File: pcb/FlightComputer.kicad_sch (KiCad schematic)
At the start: 80 parts, among them J1 USB4105-GF-A, J2 MOTOR L, J3 MOTOR R, J4 LED L, J7 SERVO R, J8 SERVO R, Q1 DMG3415U, Q2 Si2319CDS, Q3 Si2319CDS, Q4 MMBT3904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

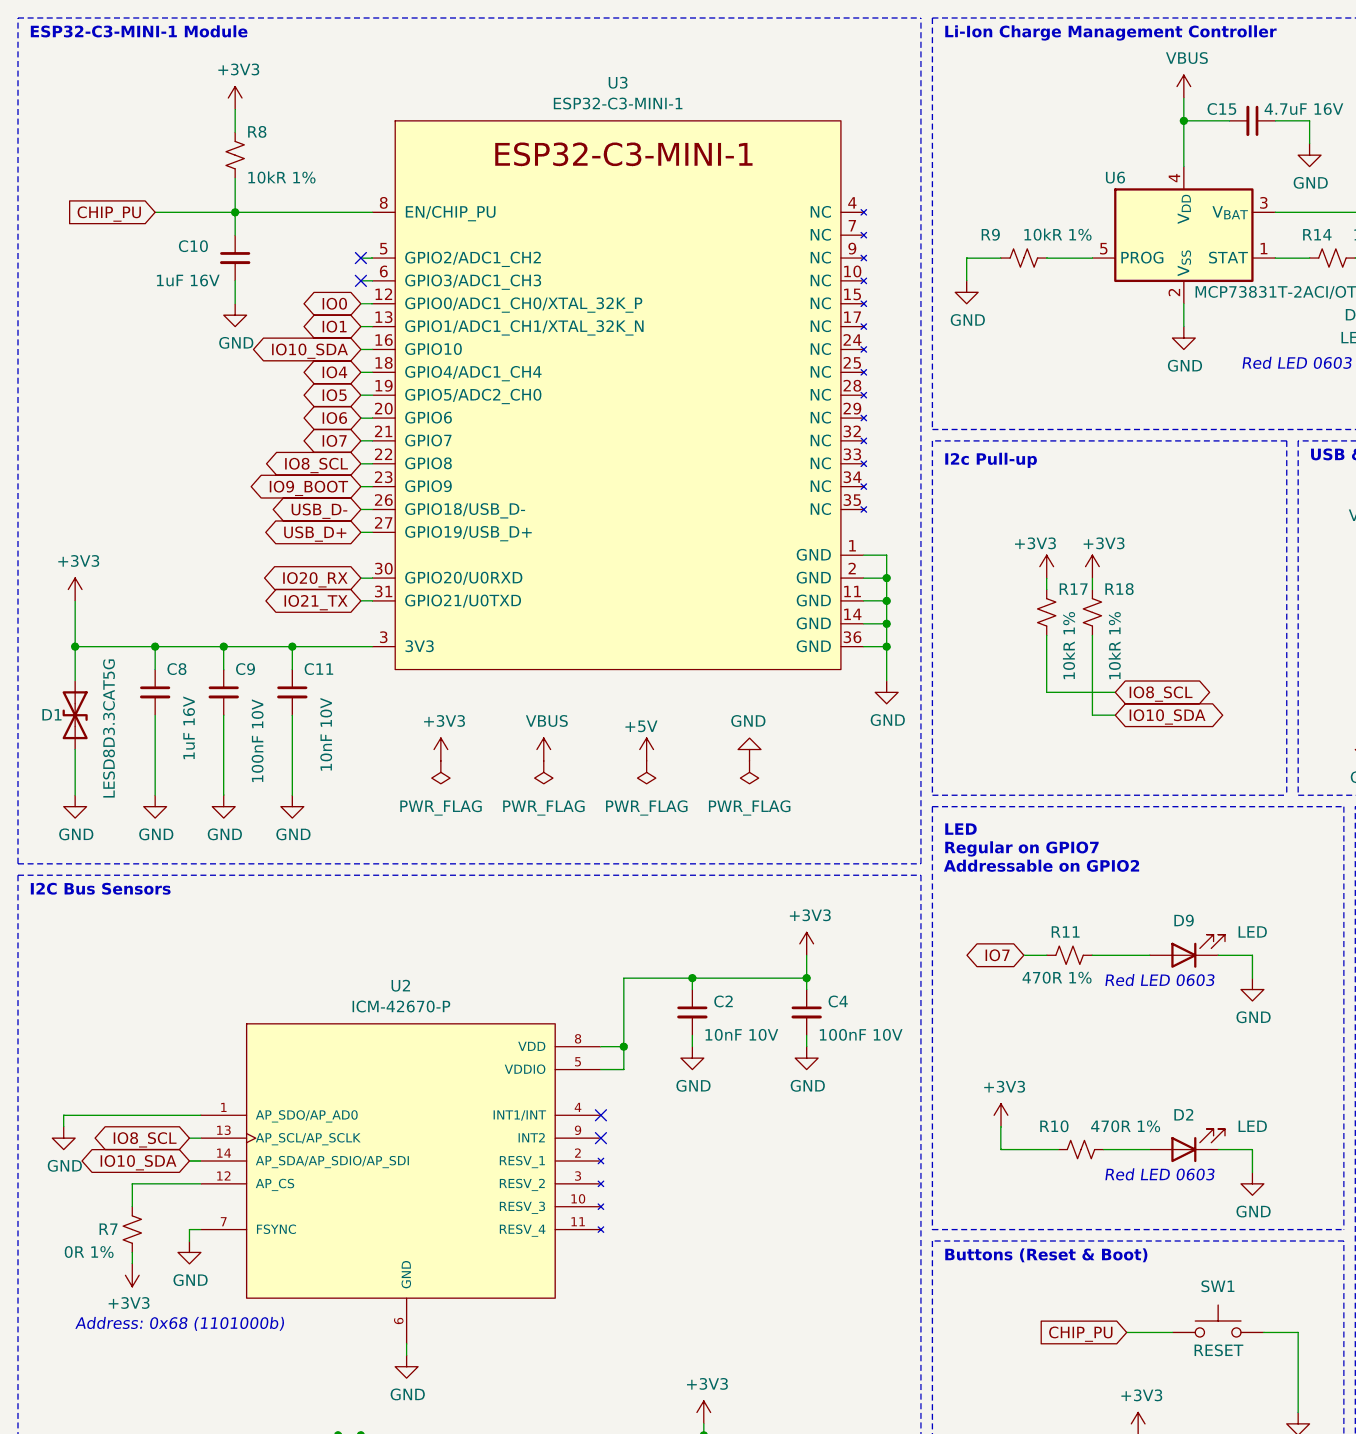
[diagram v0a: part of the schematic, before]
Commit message: Rearrange some vias, minor changes
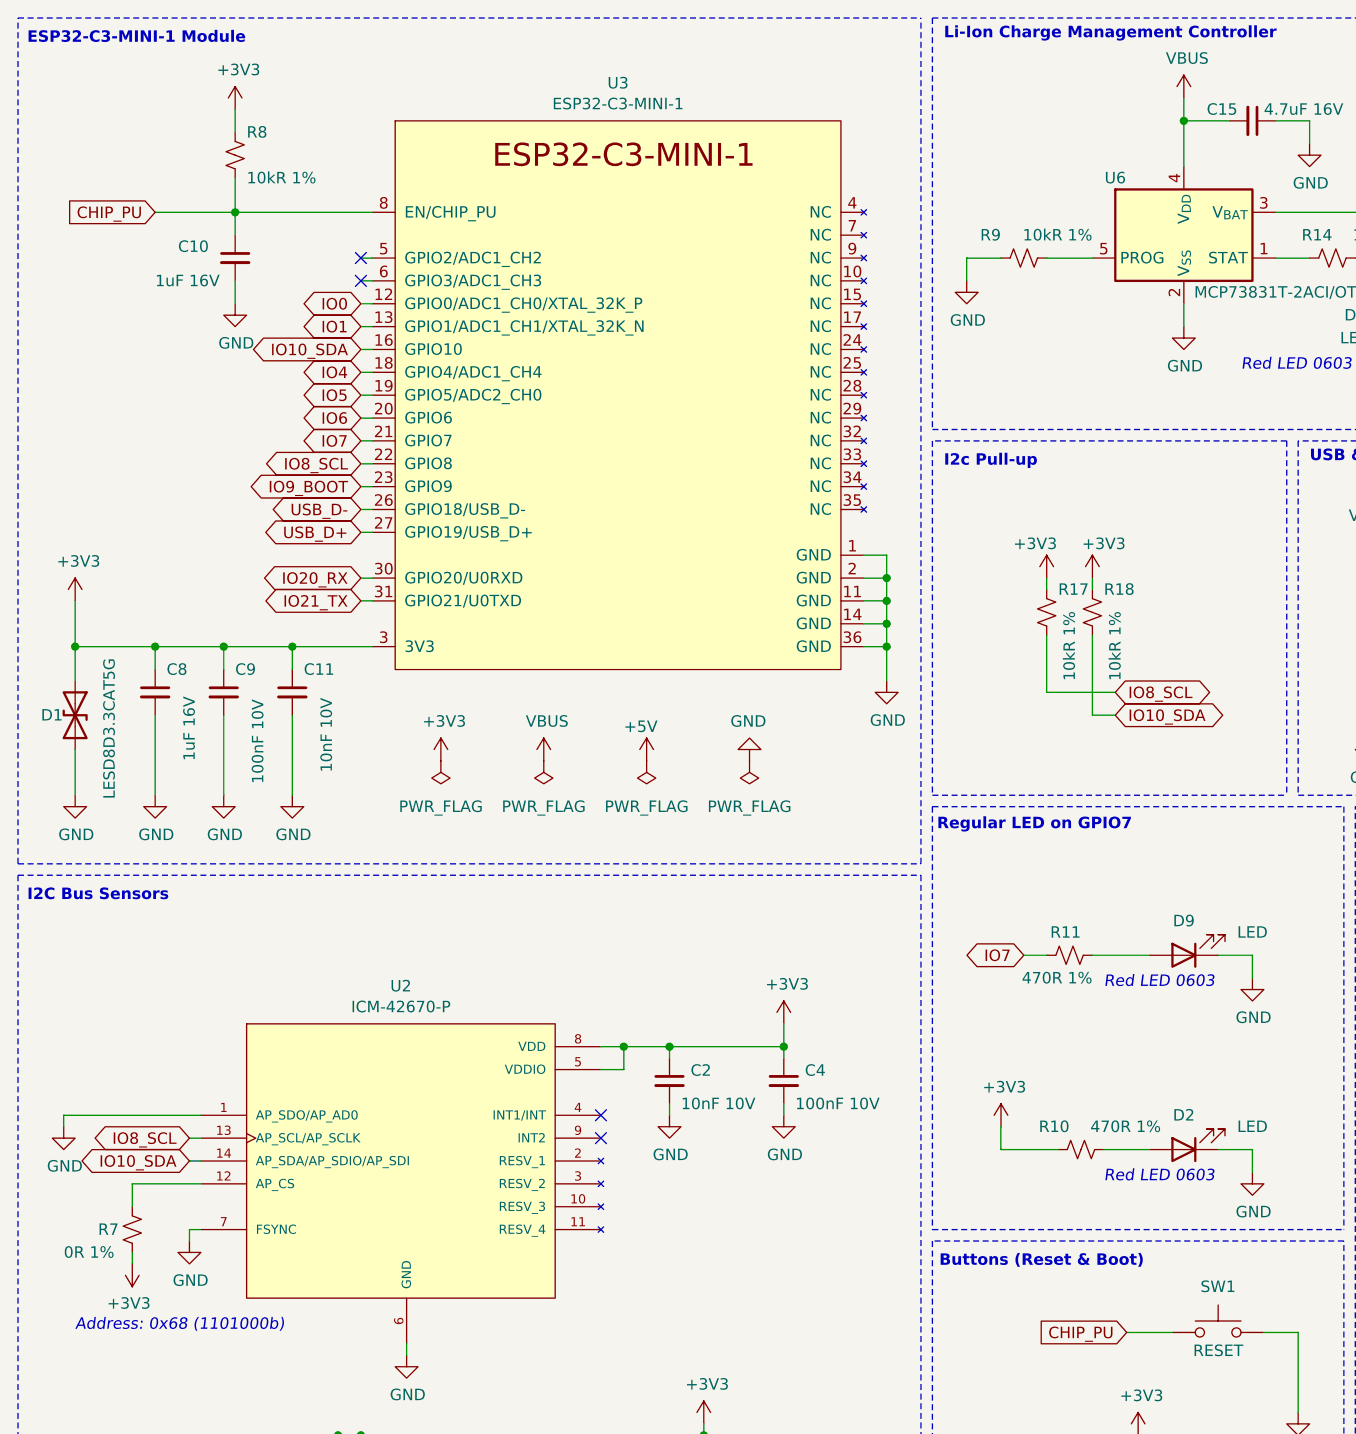
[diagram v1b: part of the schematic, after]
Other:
- note added: "Regular LED on GPIO7"
- note removed: "LED Regular on GPIO7 Addressable on GPIO2"
- moved on the sheet: C2, C4
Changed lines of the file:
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@@
 	)
 	(junction
-		(at 87.63 120.65)
+		(at 85.09 128.27)
 		(diameter 0)
 		(color 0 0 0 0)
@@
 	)
 	(junction
-		(at 100.33 120.65)
+		(at 97.79 128.27)
 		(diameter 0)
 		(color 0 0 0 0)
@@
 	(wire
 		(pts
-			(xy 100.33 120.65) (xy 87.63 120.65)
+			(xy 97.79 128.27) (xy 85.09 128.27)
 		)
 		(stroke
@@
 	(wire
 		(pts
-			(xy 100.33 118.11) (xy 100.33 120.65)
+			(xy 97.79 125.73) (xy 97.79 128.27)
 		)
 		(stroke
@@
 	(wire
 		(pts
-			(xy 100.33 127) (xy 100.33 128.27)
+			(xy 97.79 134.62) (xy 97.79 135.89)
 		)
 		(stroke
@@
 	(wire
 		(pts
-			(xy 100.33 121.92) (xy 100.33 120.65)
+			(xy 97.79 129.54) (xy 97.79 128.27)
 		)
 		(stroke
@@
 	(wire
 		(pts
-			(xy 87.63 120.65) (xy 80.01 120.65)
+			(xy 85.09 128.27) (xy 80.01 128.27)
 		)
 		(stroke
@@
 	(wire
 		(pts
-			(xy 80.01 120.65) (xy 80.01 128.27)
-		)
-		(stroke
-			(width 0)
-			(type default)
-		)
-	)
-	(wire
-		(pts
 			(xy 78.74 248.92) (xy 80.01 248.92)
 		)
@@
 	(wire
 		(pts
-			(xy 87.63 121.92) (xy 87.63 120.65)
+			(xy 85.09 129.54) (xy 85.09 128.27)
 		)
 		(stroke
@@
 	(wire
 		(pts
-			(xy 87.63 127) (xy 87.63 128.27)
+			(xy 85.09 134.62) (xy 85.09 135.89)
 		)
 		(stroke
@@
 	(text "Buttons (Reset & Boot)"
 		(exclude_from_sim no)
-		(at 115.57 152.4 0)
+		(at 115.062 152.908 0)
 		(effects
 			(font
@@
 		)
 	)
-	(text "LED\nRegular on GPIO7\nAddressable on GPIO2"
+	(text "Regular LED on GPIO7"
 		(exclude_from_sim no)
-		(at 115.57 109.22 0)
+		(at 114.808 104.394 0)
 		(effects
 			(font
@@
 	(text "ESP32-C3-MINI-1 Module"
 		(exclude_from_sim no)
-		(at 13.97 16.51 0)
+		(at 13.716 17.018 0)
 		(effects
 			(font
@@
 	(text "I2C Bus Sensors"
 		(exclude_from_sim no)
-		(at 13.97 111.76 0)
+		(at 13.716 112.268 0)
 		(effects
 			(font
@@
 	(symbol
 		(lib_id "power:+3V3")
-		(at 100.33 118.11 0)
+		(at 97.79 125.73 0)
 		(unit 1)
 		(exclude_from_sim no)
@@
 		(dnp no)
 		(property "Reference" "#PWR0117"
-			(at 100.33 121.92 0)
+			(at 97.79 129.54 0)
 			(effects
 				(font
@@
 		)
 		(property "Value" "+3V3"
-			(at 100.711 113.7158 0)
+			(at 98.171 121.3358 0)
 			(effects
 				(font
@@
 		)
 		(property "Footprint" ""
-			(at 100.33 118.11 0)
+			(at 97.79 125.73 0)
 			(effects
 				(font
@@
 		)
 		(property "Datasheet" ""
-			(at 100.33 118.11 0)
+			(at 97.79 125.73 0)
 			(effects
 				(font
@@
 		)
 		(property "Description" "Power symbol creates a global label with name \"+3V3\""
-			(at 100.33 118.11 0)
+			(at 97.79 125.73 0)
 			(effects
 				(font
@@
 	(symbol
 		(lib_id "Device:C_Small")
-		(at 87.63 124.46 0)
+		(at 85.09 132.08 0)
 		(unit 1)
 		(exclude_from_sim no)
@@
 		(dnp no)
 		(property "Reference" "C2"
-			(at 89.9668 123.2916 0)
+			(at 87.4268 130.9116 0)
 			(effects
 				(font
@@
 		)
 		(property "Value" "10nF 10V"
-			(at 88.9 127 0)
+			(at 86.36 134.62 0)
 			(effects
 				(font
@@
 		)
 		(property "Footprint" "Capacitor_SMD:C_0402_1005Metric"
-			(at 87.63 124.46 0)
+			(at 85.09 132.08 0)
 			(effects
 				(font
@@
 		)
 		(property "Datasheet" "~"
-			(at 87.63 124.46 0)
+			(at 85.09 132.08 0)
 			(effects
 				(font
@@
 		)
 		(property "Description" ""
-			(at 87.63 124.46 0)
+			(at 85.09 132.08 0)
 			(effects
 				(font
@@
 		)
 		(property "LCSC" "C15195"
-			(at 87.63 124.46 0)
+			(at 85.09 132.08 0)
 			(effects
 				(font
@@
 	(symbol
 		(lib_id "power:GND")
-		(at 87.63 128.27 0)
+		(at 85.09 135.89 0)
 		(unit 1)
 		(exclude_from_sim no)
@@
 		(dnp no)
 		(property "Reference" "#PWR0119"
-			(at 87.63 134.62 0)
+			(at 85.09 142.24 0)
 			(effects
 				(font
@@
 		)
 		(property "Value" "GND"
-			(at 87.757 132.6642 0)
+			(at 85.217 140.2842 0)
 			(effects
 				(font
@@
 		)
 		(property "Footprint" ""
-			(at 87.63 128.27 0)
+			(at 85.09 135.89 0)
 			(effects
 				(font
@@
 		)
 		(property "Datasheet" ""
-			(at 87.63 128.27 0)
+			(at 85.09 135.89 0)
 			(effects
 				(font
@@
 		)
 		(property "Description" "Power symbol creates a global label with name \"GND\" , ground"
-			(at 87.63 128.27 0)
+			(at 85.09 135.89 0)
 			(effects
 				(font
@@
 	(symbol
 		(lib_id "Device:C_Small")
-		(at 100.33 124.46 0)
+		(at 97.79 132.08 0)
 		(unit 1)
 		(exclude_from_sim no)
@@
 		(dnp no)
 		(property "Reference" "C4"
-			(at 102.6668 123.2916 0)
+			(at 100.1268 130.9116 0)
 			(effects
 				(font
@@
 		)
 		(property "Value" "100nF 10V"
-			(at 101.6 127 0)
+			(at 99.06 134.62 0)
 			(effects
 				(font
@@
 		)
 		(property "Footprint" "Capacitor_SMD:C_0402_1005Metric"
-			(at 100.33 124.46 0)
+			(at 97.79 132.08 0)
 			(effects
 				(font
@@
 		)
 		(property "Datasheet" "~"
-			(at 100.33 124.46 0)
+			(at 97.79 132.08 0)
 			(effects
 				(font
@@
 		)
 		(property "Description" ""
-			(at 100.33 124.46 0)
+			(at 97.79 132.08 0)
 			(effects
 				(font
@@
 		)
 		(property "LCSC" "C1525"
-			(at 100.33 124.46 0)
+			(at 97.79 132.08 0)
 			(effects
 				(font
@@
 	(symbol
 		(lib_id "power:GND")
-		(at 100.33 128.27 0)
+		(at 97.79 135.89 0)
 		(unit 1)
 		(exclude_from_sim no)
@@
 		(dnp no)
 		(property "Reference" "#PWR0120"
-			(at 100.33 134.62 0)
+			(at 97.79 142.24 0)
 			(effects
 				(font
@@
 		)
 		(property "Value" "GND"
-			(at 100.457 132.6642 0)
+			(at 97.917 140.2842 0)
 			(effects
 				(font
@@
 		)
 		(property "Footprint" ""
-			(at 100.33 128.27 0)
+			(at 97.79 135.89 0)
 			(effects
 				(font
@@
 		)
 		(property "Datasheet" ""
-			(at 100.33 128.27 0)
+			(at 97.79 135.89 0)
 			(effects
 				(font
@@
 		)
 		(property "Description" "Power symbol creates a global label with name \"GND\" , ground"
-			(at 100.33 128.27 0)
+			(at 97.79 135.89 0)
 			(effects
 				(font

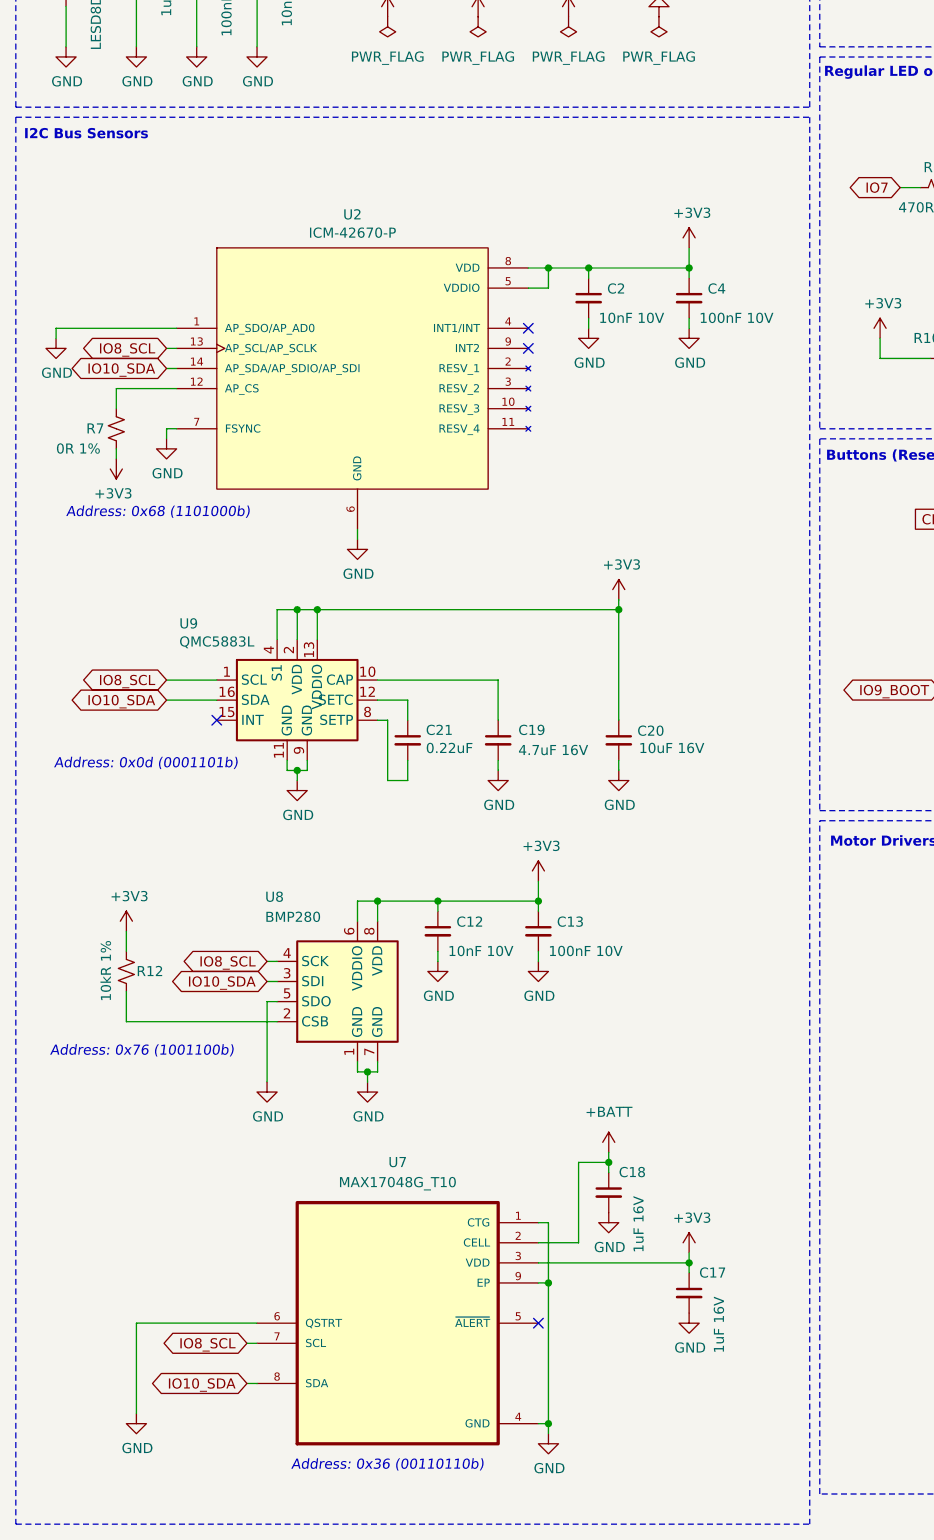
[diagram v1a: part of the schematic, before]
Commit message: BMP280 > BMP388
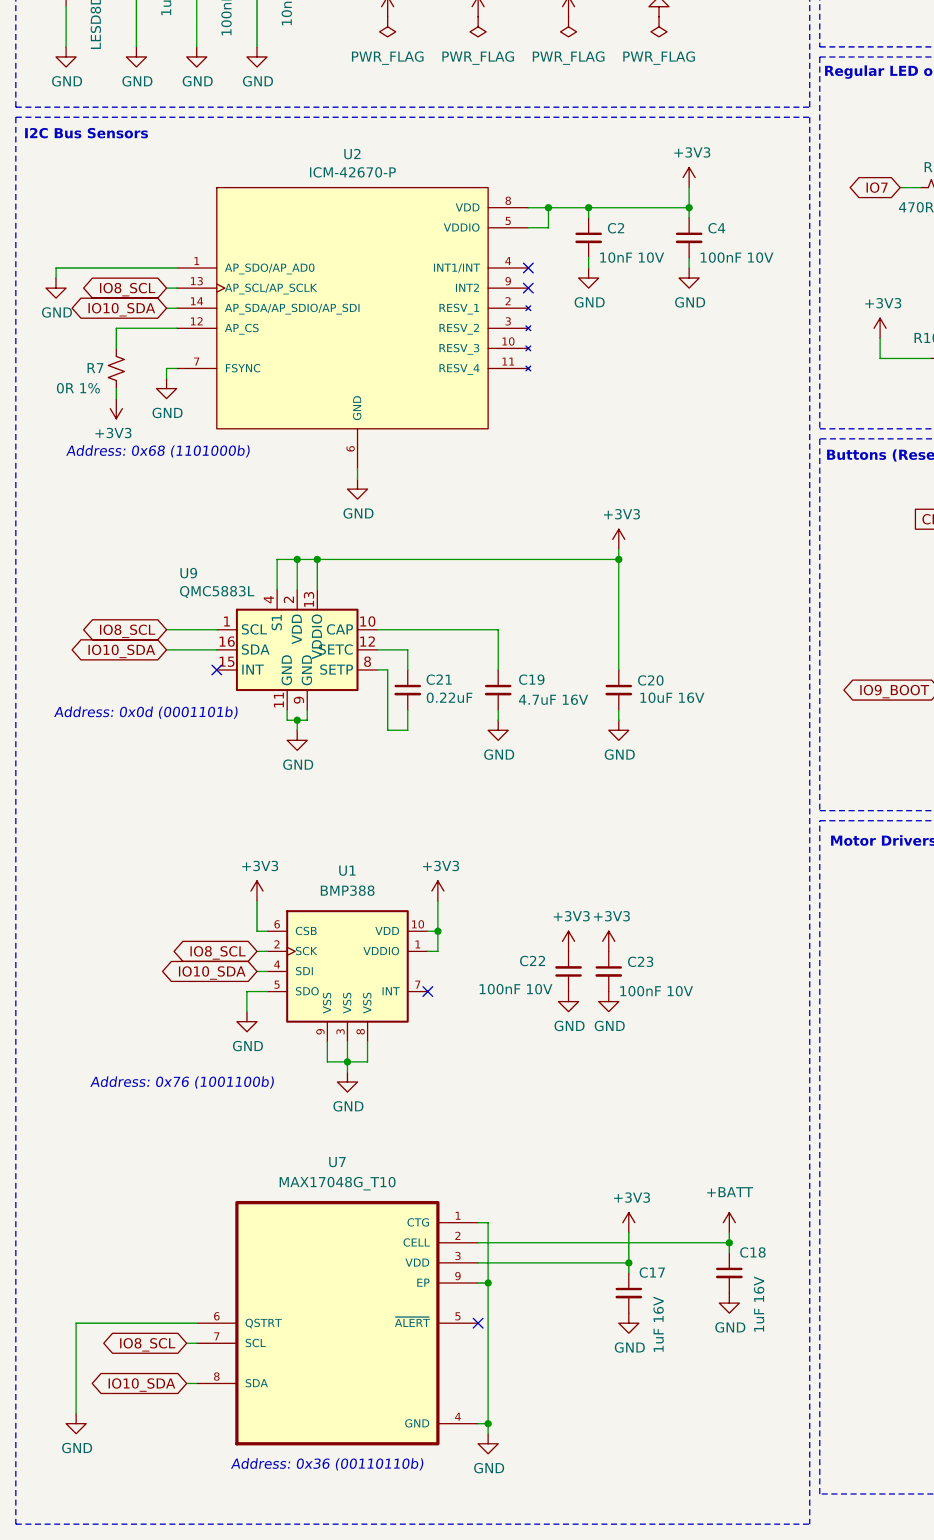
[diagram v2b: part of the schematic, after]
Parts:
- removed C12: 10nF 10V, Capacitor_SMD:C_0402_1005Metric, symbol Device:C_Small
- removed C13: 100nF 10V, Capacitor_SMD:C_0402_1005Metric, symbol Device:C_Small
- removed R12: 10kR 1%, Resistor_SMD:R_0402_1005Metric, symbol Device:R_Small_US
- removed U8: BMP280, Package_LGA:Bosch_LGA-8_2x2.5mm_P0.65mm_ClockwisePinNumbering, symbol Sensor_Pressure:BMP280
- added C22, C23: 100nF 10V, Capacitor_SMD:C_0402_1005Metric, symbol Device:C_Small
- added U1: BMP388, Package_LGA:Rohm_MLGA010V020A_LGA-10_2x2mm_P0.45mm_LayoutBorder2x3y, symbol Rust_Board:BMP388
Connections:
- net +3V3: now also C22.2, C23.1, U1.1 (VDDIO), U1.10 (VDD), U1.6 (CSB)
- net GND: now also C22.1, C23.2, U1.3 (VSS), U1.5 (SDO), U1.8 (VSS), U1.9 (VSS)
- net IO10_SDA: now also U1.4 (SDI)
- net IO8_SCL: now also U1.2 (SCK)
- no-connect marks 9 -> 10
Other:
- moved on the sheet: C17, C18, C19, C2, C20, C21, C4, R7, U2, U7, U9
